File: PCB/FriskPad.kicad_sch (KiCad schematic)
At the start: 11 parts, among them J1 Conn_01x04, SW1 SW_Push, SW2 SW_Push, SW3 SW_Push, SW4 SW_Push, SW5 SW_Push, SW6 SW_Push, SW7 SW_Push, SW8 SW_Push, SW9 SW_Push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

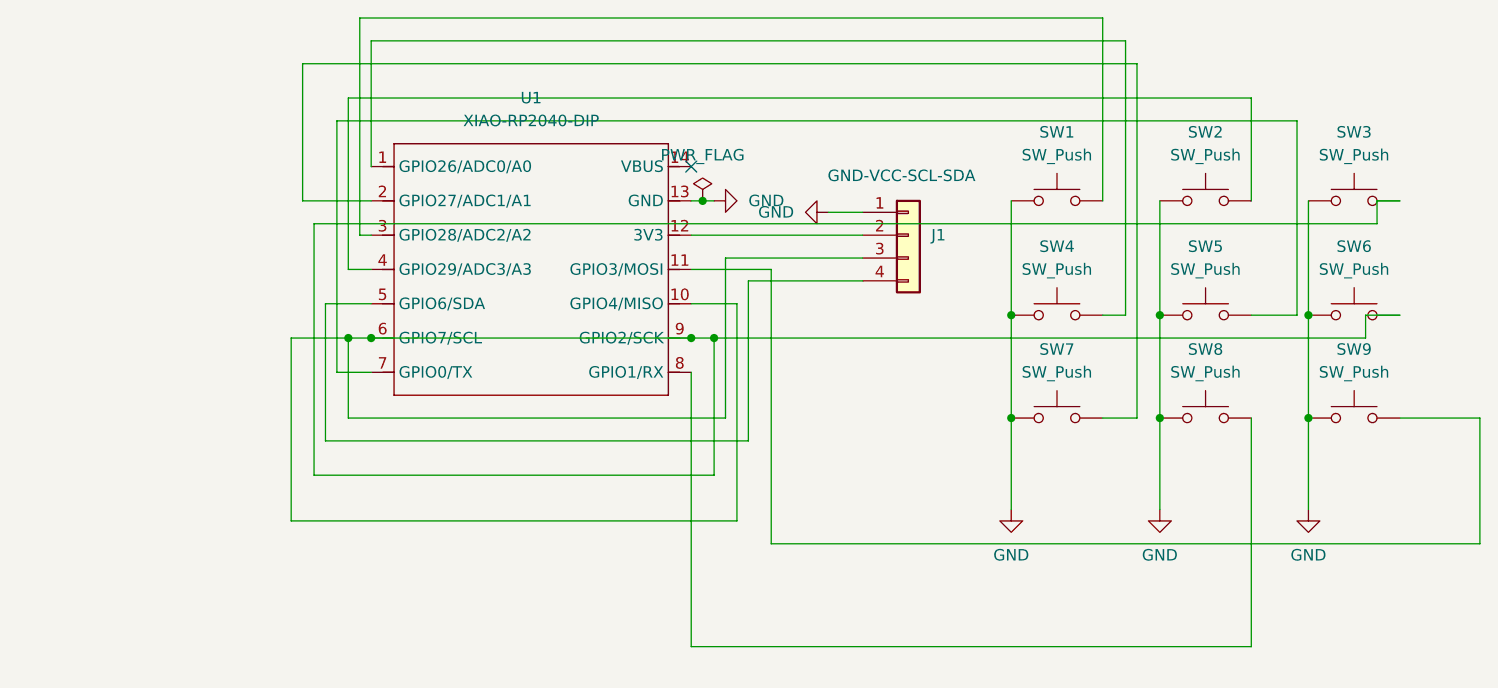
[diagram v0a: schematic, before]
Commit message: Changes improving schematics design
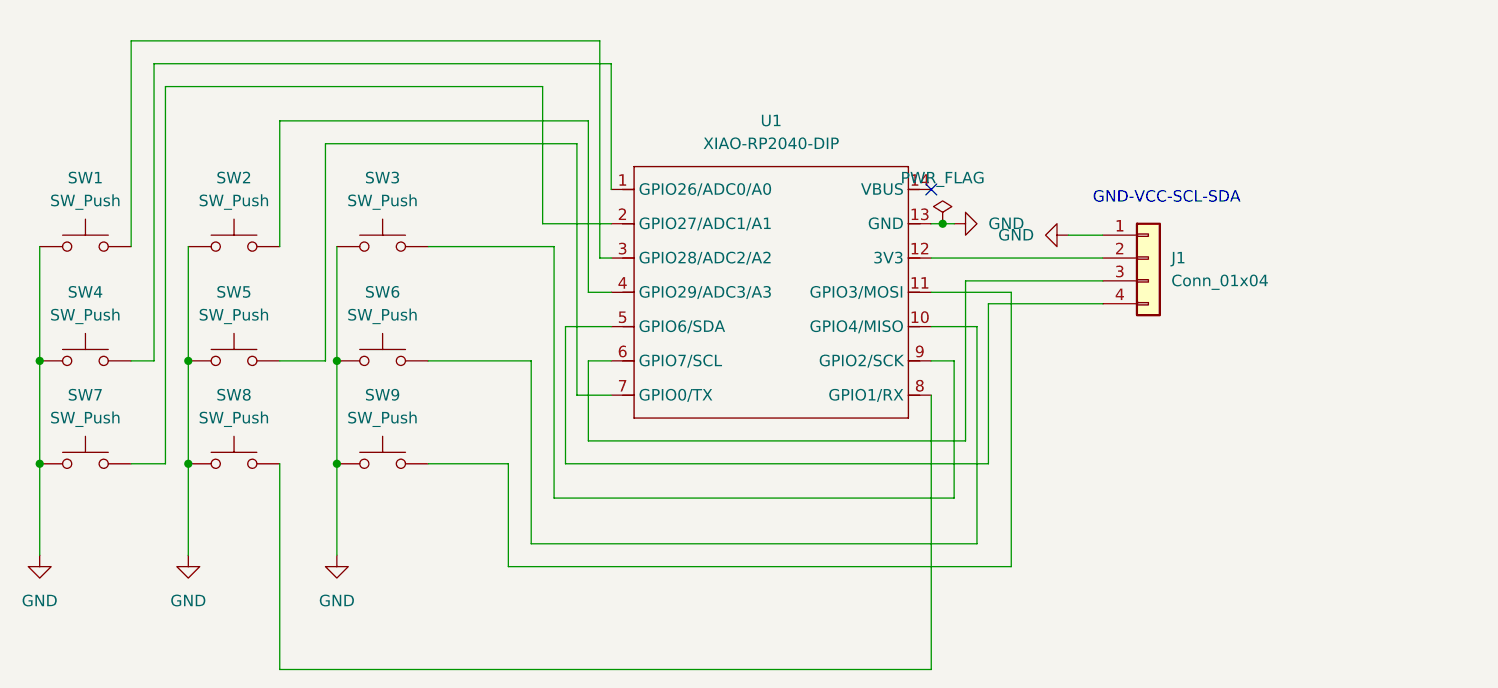
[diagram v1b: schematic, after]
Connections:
- new net: SW6.2, U1.10 (GPIO4/MISO)
- new net: J1.3 (Pin_3), U1.6 (GPIO7/SCL)
- new net: SW3.2, U1.9 (GPIO2/SCK)
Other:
- moved on the sheet: J1, SW1, SW2, SW3, SW4, SW5, SW6, SW7, SW8, SW9, U1
